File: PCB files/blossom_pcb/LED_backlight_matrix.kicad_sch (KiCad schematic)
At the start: 17 parts

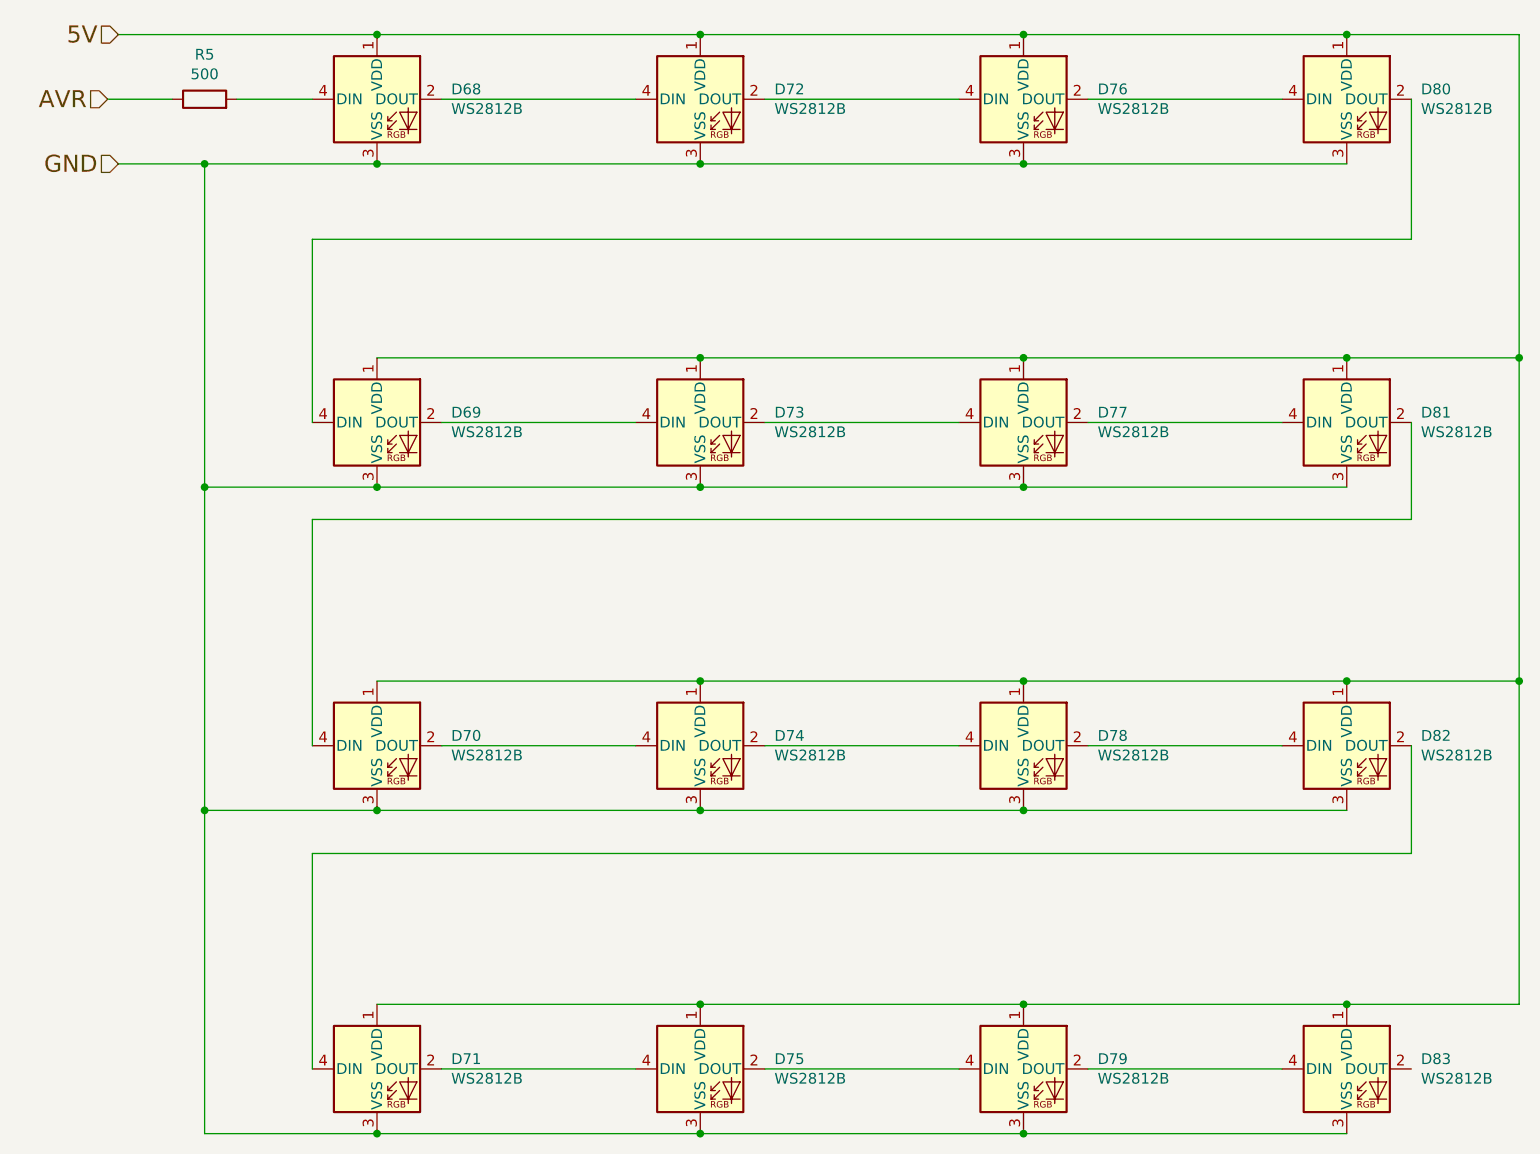
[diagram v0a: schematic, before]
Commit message: added rp2040, need to update footprints
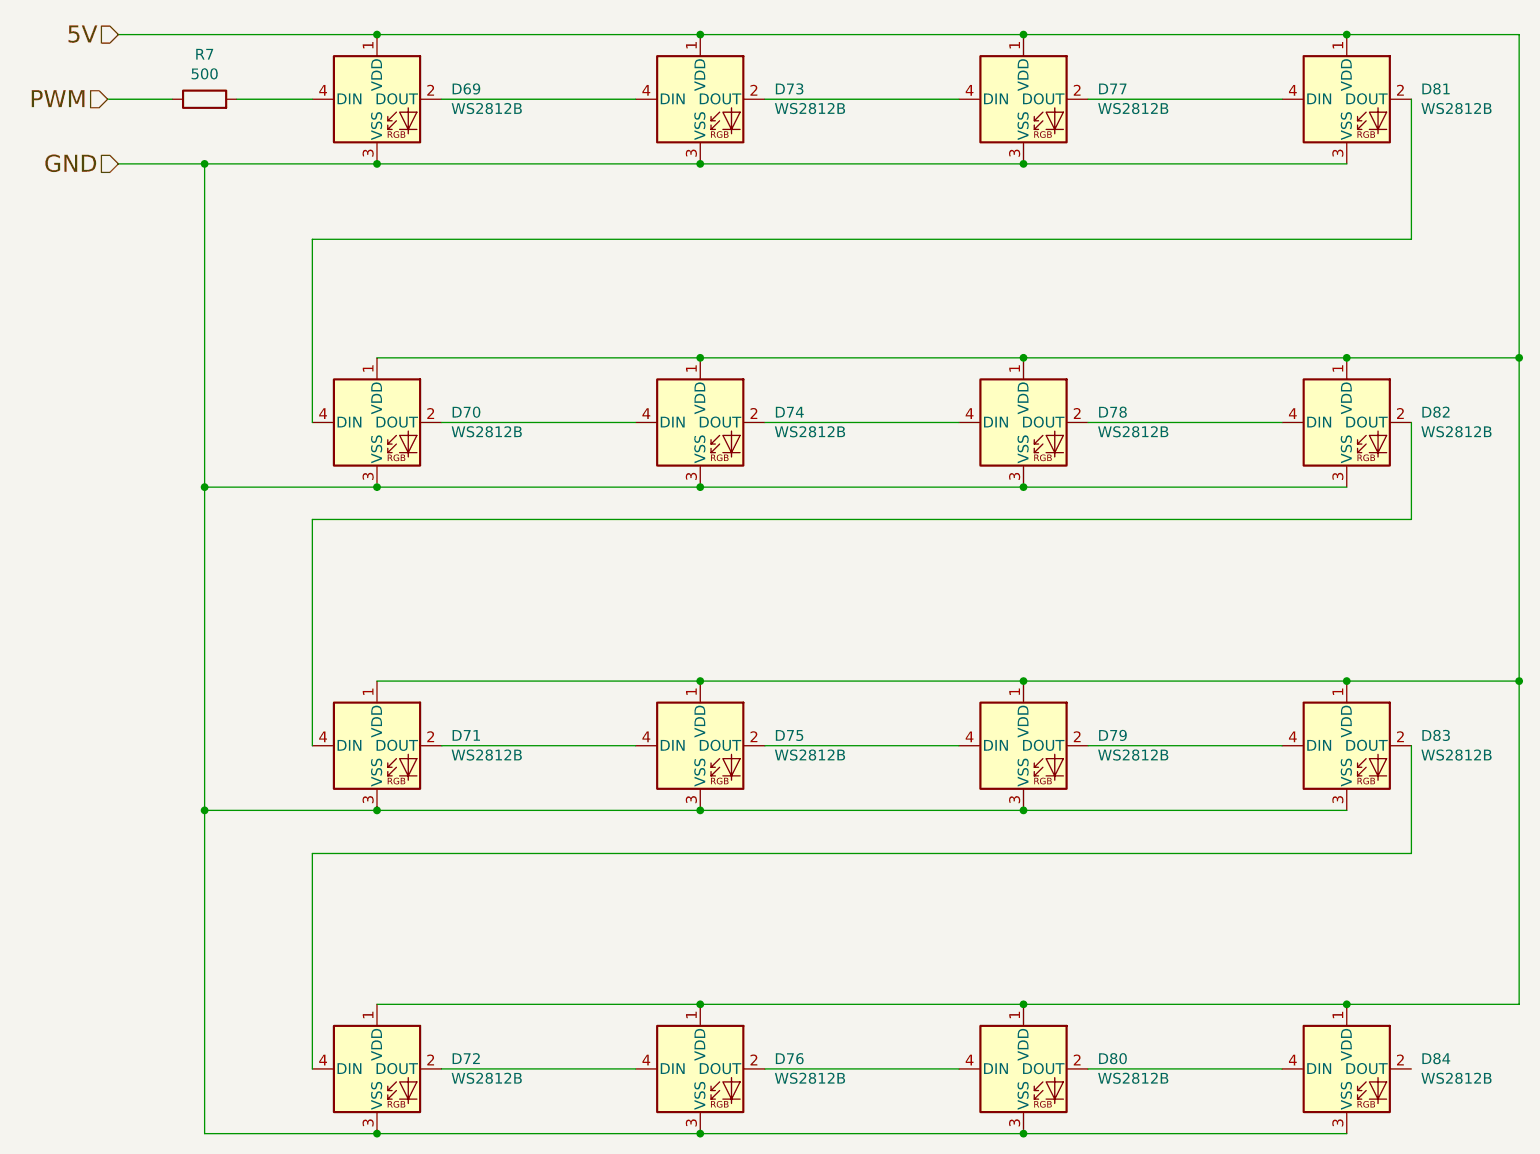
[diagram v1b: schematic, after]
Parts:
- D69: renamed from D68; symbol LED:WS2812B -> arisu-rescue:WS2812B-LED
- D70: renamed from D69; symbol LED:WS2812B -> arisu-rescue:WS2812B-LED
- D71: renamed from D70; symbol LED:WS2812B -> arisu-rescue:WS2812B-LED
- D72: renamed from D71; symbol LED:WS2812B -> arisu-rescue:WS2812B-LED
- D73: renamed from D72; symbol LED:WS2812B -> arisu-rescue:WS2812B-LED
- D74: renamed from D73; symbol LED:WS2812B -> arisu-rescue:WS2812B-LED
- D75: renamed from D74; symbol LED:WS2812B -> arisu-rescue:WS2812B-LED
- D76: renamed from D75; symbol LED:WS2812B -> arisu-rescue:WS2812B-LED
- D77: renamed from D76; symbol LED:WS2812B -> arisu-rescue:WS2812B-LED
- D78: renamed from D77; symbol LED:WS2812B -> arisu-rescue:WS2812B-LED
- D79: renamed from D78; symbol LED:WS2812B -> arisu-rescue:WS2812B-LED
- D80: renamed from D79; symbol LED:WS2812B -> arisu-rescue:WS2812B-LED
- D81: renamed from D80; symbol LED:WS2812B -> arisu-rescue:WS2812B-LED
- D82: renamed from D81; symbol LED:WS2812B -> arisu-rescue:WS2812B-LED
- D83: renamed from D82; symbol LED:WS2812B -> arisu-rescue:WS2812B-LED
- D84: renamed from D83; symbol LED:WS2812B -> arisu-rescue:WS2812B-LED
- R7: renamed from R5; symbol Device:R -> arisu-rescue:R-Device
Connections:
- net AVR renamed PWM

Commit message: Almost doing stuffs
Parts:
- renumbered D69 to D101, D73 to D102, D77 to D103, D81 to D104, D70 to D105, D74 to D106, D78 to D107, D82 to D108, D71 to D109, D75 to D110, D79 to D111, D83 to D112, D72 to D113, D76 to D114, D80 to D115, D84 to D116, R7 to R101
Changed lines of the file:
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@@
   (symbol (lib_id "arisu-rescue:WS2812B-LED") (at 139.7 30.48 0) (unit 1)
     (in_bom yes) (on_board yes) (dnp no)
-    (property "Reference" "D69" (at 148.4376 29.3116 0)
+    (property "Reference" "D101" (at 148.4376 29.3116 0)
       (effects (font (size 1.27 1.27)) (justify left))
     )
@@
       (project "arisu"
         (path "/6a4507f9-fb93-401b-b9e1-9f2bcbbd5186/00000000-0000-0000-0000-000060e58188"
-          (reference "D69") (unit 1)
+          (reference "D101") (unit 1)
         )
       )
@@
   (symbol (lib_id "arisu-rescue:WS2812B-LED") (at 177.8 30.48 0) (unit 1)
     (in_bom yes) (on_board yes) (dnp no)
-    (property "Reference" "D73" (at 186.5376 29.3116 0)
+    (property "Reference" "D102" (at 186.5376 29.3116 0)
       (effects (font (size 1.27 1.27)) (justify left))
     )
@@
       (project "arisu"
         (path "/6a4507f9-fb93-401b-b9e1-9f2bcbbd5186/00000000-0000-0000-0000-000060e58188"
-          (reference "D73") (unit 1)
+          (reference "D102") (unit 1)
         )
       )
@@
   (symbol (lib_id "arisu-rescue:WS2812B-LED") (at 139.7 68.58 0) (unit 1)
     (in_bom yes) (on_board yes) (dnp no)
-    (property "Reference" "D70" (at 148.4376 67.4116 0)
+    (property "Reference" "D105" (at 148.4376 67.4116 0)
       (effects (font (size 1.27 1.27)) (justify left))
     )
@@
       (project "arisu"
         (path "/6a4507f9-fb93-401b-b9e1-9f2bcbbd5186/00000000-0000-0000-0000-000060e58188"
-          (reference "D70") (unit 1)
+          (reference "D105") (unit 1)
         )
       )
@@
   (symbol (lib_id "arisu-rescue:WS2812B-LED") (at 177.8 68.58 0) (unit 1)
     (in_bom yes) (on_board yes) (dnp no)
-    (property "Reference" "D74" (at 186.5376 67.4116 0)
+    (property "Reference" "D106" (at 186.5376 67.4116 0)
       (effects (font (size 1.27 1.27)) (justify left))
     )
@@
       (project "arisu"
         (path "/6a4507f9-fb93-401b-b9e1-9f2bcbbd5186/00000000-0000-0000-0000-000060e58188"
-          (reference "D74") (unit 1)
+          (reference "D106") (unit 1)
         )
       )
@@
   (symbol (lib_id "arisu-rescue:WS2812B-LED") (at 215.9 30.48 0) (unit 1)
     (in_bom yes) (on_board yes) (dnp no)
-    (property "Reference" "D77" (at 224.6376 29.3116 0)
+    (property "Reference" "D103" (at 224.6376 29.3116 0)
       (effects (font (size 1.27 1.27)) (justify left))
     )
@@
       (project "arisu"
         (path "/6a4507f9-fb93-401b-b9e1-9f2bcbbd5186/00000000-0000-0000-0000-000060e58188"
-          (reference "D77") (unit 1)
+          (reference "D103") (unit 1)
         )
       )
@@
   (symbol (lib_id "arisu-rescue:WS2812B-LED") (at 254 30.48 0) (unit 1)
     (in_bom yes) (on_board yes) (dnp no)
-    (property "Reference" "D81" (at 262.7376 29.3116 0)
+    (property "Reference" "D104" (at 262.7376 29.3116 0)
       (effects (font (size 1.27 1.27)) (justify left))
     )
@@
       (project "arisu"
         (path "/6a4507f9-fb93-401b-b9e1-9f2bcbbd5186/00000000-0000-0000-0000-000060e58188"
-          (reference "D81") (unit 1)
+          (reference "D104") (unit 1)
         )
       )
@@
   (symbol (lib_id "arisu-rescue:WS2812B-LED") (at 215.9 68.58 0) (unit 1)
     (in_bom yes) (on_board yes) (dnp no)
-    (property "Reference" "D78" (at 224.6376 67.4116 0)
+    (property "Reference" "D107" (at 224.6376 67.4116 0)
       (effects (font (size 1.27 1.27)) (justify left))
     )
@@
       (project "arisu"
         (path "/6a4507f9-fb93-401b-b9e1-9f2bcbbd5186/00000000-0000-0000-0000-000060e58188"
-          (reference "D78") (unit 1)
+          (reference "D107") (unit 1)
         )
       )
@@
   (symbol (lib_id "arisu-rescue:WS2812B-LED") (at 254 68.58 0) (unit 1)
     (in_bom yes) (on_board yes) (dnp no)
-    (property "Reference" "D82" (at 262.7376 67.4116 0)
+    (property "Reference" "D108" (at 262.7376 67.4116 0)
       (effects (font (size 1.27 1.27)) (justify left))
     )
@@
       (project "arisu"
         (path "/6a4507f9-fb93-401b-b9e1-9f2bcbbd5186/00000000-0000-0000-0000-000060e58188"
-          (reference "D82") (unit 1)
+          (reference "D108") (unit 1)
         )
       )
@@
   (symbol (lib_id "arisu-rescue:WS2812B-LED") (at 139.7 106.68 0) (unit 1)
     (in_bom yes) (on_board yes) (dnp no)
-    (property "Reference" "D71" (at 148.4376 105.5116 0)
+    (property "Reference" "D109" (at 148.4376 105.5116 0)
       (effects (font (size 1.27 1.27)) (justify left))
     )
@@
       (project "arisu"
         (path "/6a4507f9-fb93-401b-b9e1-9f2bcbbd5186/00000000-0000-0000-0000-000060e58188"
-          (reference "D71") (unit 1)
+          (reference "D109") (unit 1)
         )
       )
@@
   (symbol (lib_id "arisu-rescue:WS2812B-LED") (at 177.8 106.68 0) (unit 1)
     (in_bom yes) (on_board yes) (dnp no)
-    (property "Reference" "D75" (at 186.5376 105.5116 0)
+    (property "Reference" "D110" (at 186.5376 105.5116 0)
       (effects (font (size 1.27 1.27)) (justify left))
     )
@@
       (project "arisu"
         (path "/6a4507f9-fb93-401b-b9e1-9f2bcbbd5186/00000000-0000-0000-0000-000060e58188"
-          (reference "D75") (unit 1)
+          (reference "D110") (unit 1)
         )
       )
@@
   (symbol (lib_id "arisu-rescue:WS2812B-LED") (at 139.7 144.78 0) (unit 1)
     (in_bom yes) (on_board yes) (dnp no)
-    (property "Reference" "D72" (at 148.4376 143.6116 0)
+    (property "Reference" "D113" (at 148.4376 143.6116 0)
       (effects (font (size 1.27 1.27)) (justify left))
     )
@@
       (project "arisu"
         (path "/6a4507f9-fb93-401b-b9e1-9f2bcbbd5186/00000000-0000-0000-0000-000060e58188"
-          (reference "D72") (unit 1)
+          (reference "D113") (unit 1)
         )
       )
@@
   (symbol (lib_id "arisu-rescue:WS2812B-LED") (at 177.8 144.78 0) (unit 1)
     (in_bom yes) (on_board yes) (dnp no)
-    (property "Reference" "D76" (at 186.5376 143.6116 0)
+    (property "Reference" "D114" (at 186.5376 143.6116 0)
       (effects (font (size 1.27 1.27)) (justify left))
     )
@@
       (project "arisu"
         (path "/6a4507f9-fb93-401b-b9e1-9f2bcbbd5186/00000000-0000-0000-0000-000060e58188"
-          (reference "D76") (unit 1)
+          (reference "D114") (unit 1)
         )
       )
@@
   (symbol (lib_id "arisu-rescue:WS2812B-LED") (at 215.9 106.68 0) (unit 1)
     (in_bom yes) (on_board yes) (dnp no)
-    (property "Reference" "D79" (at 224.6376 105.5116 0)
+    (property "Reference" "D111" (at 224.6376 105.5116 0)
       (effects (font (size 1.27 1.27)) (justify left))
     )
@@
       (project "arisu"
         (path "/6a4507f9-fb93-401b-b9e1-9f2bcbbd5186/00000000-0000-0000-0000-000060e58188"
-          (reference "D79") (unit 1)
+          (reference "D111") (unit 1)
         )
       )
@@
   (symbol (lib_id "arisu-rescue:WS2812B-LED") (at 254 106.68 0) (unit 1)
     (in_bom yes) (on_board yes) (dnp no)
-    (property "Reference" "D83" (at 262.7376 105.5116 0)
+    (property "Reference" "D112" (at 262.7376 105.5116 0)
       (effects (font (size 1.27 1.27)) (justify left))
     )
@@
       (project "arisu"
         (path "/6a4507f9-fb93-401b-b9e1-9f2bcbbd5186/00000000-0000-0000-0000-000060e58188"
-          (reference "D83") (unit 1)
+          (reference "D112") (unit 1)
         )
       )
@@
   (symbol (lib_id "arisu-rescue:WS2812B-LED") (at 215.9 144.78 0) (unit 1)
     (in_bom yes) (on_board yes) (dnp no)
-    (property "Reference" "D80" (at 224.6376 143.6116 0)
+    (property "Reference" "D115" (at 224.6376 143.6116 0)
       (effects (font (size 1.27 1.27)) (justify left))
     )
@@
       (project "arisu"
         (path "/6a4507f9-fb93-401b-b9e1-9f2bcbbd5186/00000000-0000-0000-0000-000060e58188"
-          (reference "D80") (unit 1)
+          (reference "D115") (unit 1)
         )
       )
@@
   (symbol (lib_id "arisu-rescue:WS2812B-LED") (at 254 144.78 0) (unit 1)
     (in_bom yes) (on_board yes) (dnp no)
-    (property "Reference" "D84" (at 262.7376 143.6116 0)
+    (property "Reference" "D116" (at 262.7376 143.6116 0)
       (effects (font (size 1.27 1.27)) (justify left))
     )
@@
       (project "arisu"
         (path "/6a4507f9-fb93-401b-b9e1-9f2bcbbd5186/00000000-0000-0000-0000-000060e58188"
-          (reference "D84") (unit 1)
+          (reference "D116") (unit 1)
         )
       )
@@
   (symbol (lib_id "arisu-rescue:R-Device") (at 119.38 30.48 90) (unit 1)
     (in_bom yes) (on_board yes) (dnp no)
-    (property "Reference" "R7" (at 119.38 25.2222 90)
+    (property "Reference" "R101" (at 119.38 25.2222 90)
       (effects (font (size 1.27 1.27)))
     )
@@
       (project "arisu"
         (path "/6a4507f9-fb93-401b-b9e1-9f2bcbbd5186/00000000-0000-0000-0000-000060e58188"
-          (reference "R7") (unit 1)
-        )
-      )
+          (reference "R101") (unit 1)
+        )
+      )

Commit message: Almost complete
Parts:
- removed D109, D110, D111, D112, D113, D114, D115, D116: WS2812B, LED_SMD:LED_WS2812B_PLCC4_5.0x5.0mm_P3.2mm, symbol arisu-rescue:WS2812B-LED

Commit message: Fixed part numbers for JLCPCB
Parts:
- renumbered D101 to LED1, D102 to LED2, D103 to LED3, D104 to LED4, D105 to LED5, D106 to LED6, D107 to LED7, D108 to LED8
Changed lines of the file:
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@@
   (symbol (lib_id "arisu-rescue:WS2812B-LED") (at 139.7 30.48 0) (unit 1)
     (in_bom yes) (on_board yes) (dnp no)
-    (property "Reference" "D101" (at 148.4376 29.3116 0)
+    (property "Reference" "LED1" (at 148.4376 29.3116 0)
       (effects (font (size 1.27 1.27)) (justify left))
     )
@@
       (project "arisu"
         (path "/6a4507f9-fb93-401b-b9e1-9f2bcbbd5186/00000000-0000-0000-0000-000060e58188"
-          (reference "D101") (unit 1)
+          (reference "LED1") (unit 1)
         )
       )
@@
   (symbol (lib_id "arisu-rescue:WS2812B-LED") (at 177.8 30.48 0) (unit 1)
     (in_bom yes) (on_board yes) (dnp no)
-    (property "Reference" "D102" (at 186.5376 29.3116 0)
+    (property "Reference" "LED2" (at 186.5376 29.3116 0)
       (effects (font (size 1.27 1.27)) (justify left))
     )
@@
       (project "arisu"
         (path "/6a4507f9-fb93-401b-b9e1-9f2bcbbd5186/00000000-0000-0000-0000-000060e58188"
-          (reference "D102") (unit 1)
+          (reference "LED2") (unit 1)
         )
       )
@@
   (symbol (lib_id "arisu-rescue:WS2812B-LED") (at 139.7 68.58 0) (unit 1)
     (in_bom yes) (on_board yes) (dnp no)
-    (property "Reference" "D105" (at 148.4376 67.4116 0)
+    (property "Reference" "LED5" (at 148.4376 67.4116 0)
       (effects (font (size 1.27 1.27)) (justify left))
     )
@@
       (project "arisu"
         (path "/6a4507f9-fb93-401b-b9e1-9f2bcbbd5186/00000000-0000-0000-0000-000060e58188"
-          (reference "D105") (unit 1)
+          (reference "LED5") (unit 1)
         )
       )
@@
   (symbol (lib_id "arisu-rescue:WS2812B-LED") (at 177.8 68.58 0) (unit 1)
     (in_bom yes) (on_board yes) (dnp no)
-    (property "Reference" "D106" (at 186.5376 67.4116 0)
+    (property "Reference" "LED6" (at 186.5376 67.4116 0)
       (effects (font (size 1.27 1.27)) (justify left))
     )
@@
       (project "arisu"
         (path "/6a4507f9-fb93-401b-b9e1-9f2bcbbd5186/00000000-0000-0000-0000-000060e58188"
-          (reference "D106") (unit 1)
+          (reference "LED6") (unit 1)
         )
       )
@@
   (symbol (lib_id "arisu-rescue:WS2812B-LED") (at 215.9 30.48 0) (unit 1)
     (in_bom yes) (on_board yes) (dnp no)
-    (property "Reference" "D103" (at 224.6376 29.3116 0)
+    (property "Reference" "LED3" (at 224.6376 29.3116 0)
       (effects (font (size 1.27 1.27)) (justify left))
     )
@@
       (project "arisu"
         (path "/6a4507f9-fb93-401b-b9e1-9f2bcbbd5186/00000000-0000-0000-0000-000060e58188"
-          (reference "D103") (unit 1)
+          (reference "LED3") (unit 1)
         )
       )
@@
   (symbol (lib_id "arisu-rescue:WS2812B-LED") (at 254 30.48 0) (unit 1)
     (in_bom yes) (on_board yes) (dnp no)
-    (property "Reference" "D104" (at 262.7376 29.3116 0)
+    (property "Reference" "LED4" (at 262.7376 29.3116 0)
       (effects (font (size 1.27 1.27)) (justify left))
     )
@@
       (project "arisu"
         (path "/6a4507f9-fb93-401b-b9e1-9f2bcbbd5186/00000000-0000-0000-0000-000060e58188"
-          (reference "D104") (unit 1)
+          (reference "LED4") (unit 1)
         )
       )
@@
   (symbol (lib_id "arisu-rescue:WS2812B-LED") (at 215.9 68.58 0) (unit 1)
     (in_bom yes) (on_board yes) (dnp no)
-    (property "Reference" "D107" (at 224.6376 67.4116 0)
+    (property "Reference" "LED7" (at 224.6376 67.4116 0)
       (effects (font (size 1.27 1.27)) (justify left))
     )
@@
       (project "arisu"
         (path "/6a4507f9-fb93-401b-b9e1-9f2bcbbd5186/00000000-0000-0000-0000-000060e58188"
-          (reference "D107") (unit 1)
+          (reference "LED7") (unit 1)
         )
       )
@@
   (symbol (lib_id "arisu-rescue:WS2812B-LED") (at 254 68.58 0) (unit 1)
     (in_bom yes) (on_board yes) (dnp no)
-    (property "Reference" "D108" (at 262.7376 67.4116 0)
+    (property "Reference" "LED8" (at 262.7376 67.4116 0)
       (effects (font (size 1.27 1.27)) (justify left))
     )
@@
       (project "arisu"
         (path "/6a4507f9-fb93-401b-b9e1-9f2bcbbd5186/00000000-0000-0000-0000-000060e58188"
-          (reference "D108") (unit 1)
-        )
-      )
+          (reference "LED8") (unit 1)
+        )
+      )
